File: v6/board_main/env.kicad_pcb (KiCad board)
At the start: 4 copper layers, 57.8 x 34 mm, 187 parts, among them J1 M50-3142045THT, J2 M50-3142045THT, J3 53261-0271, J4 USB4105-GF-A, J5 FEMALE_HEADER_2X1, M1 SISS23DN, M2 SISS23DN, Q1 FDN302P, U1 REF3012AIDBZR, U10 CY7C1051DV33, U2 MCP73833T-AMI/MF, U3 LTC3569EUDPBF, U4 PAC1934, U5 PAC1934, U6 W25Q16JVUXIQ, U7 RP2040, U8 SPARTAN7-LX15, U9 S25FL256S, X1 12MHz, X2 32MHz, X3 100MHz

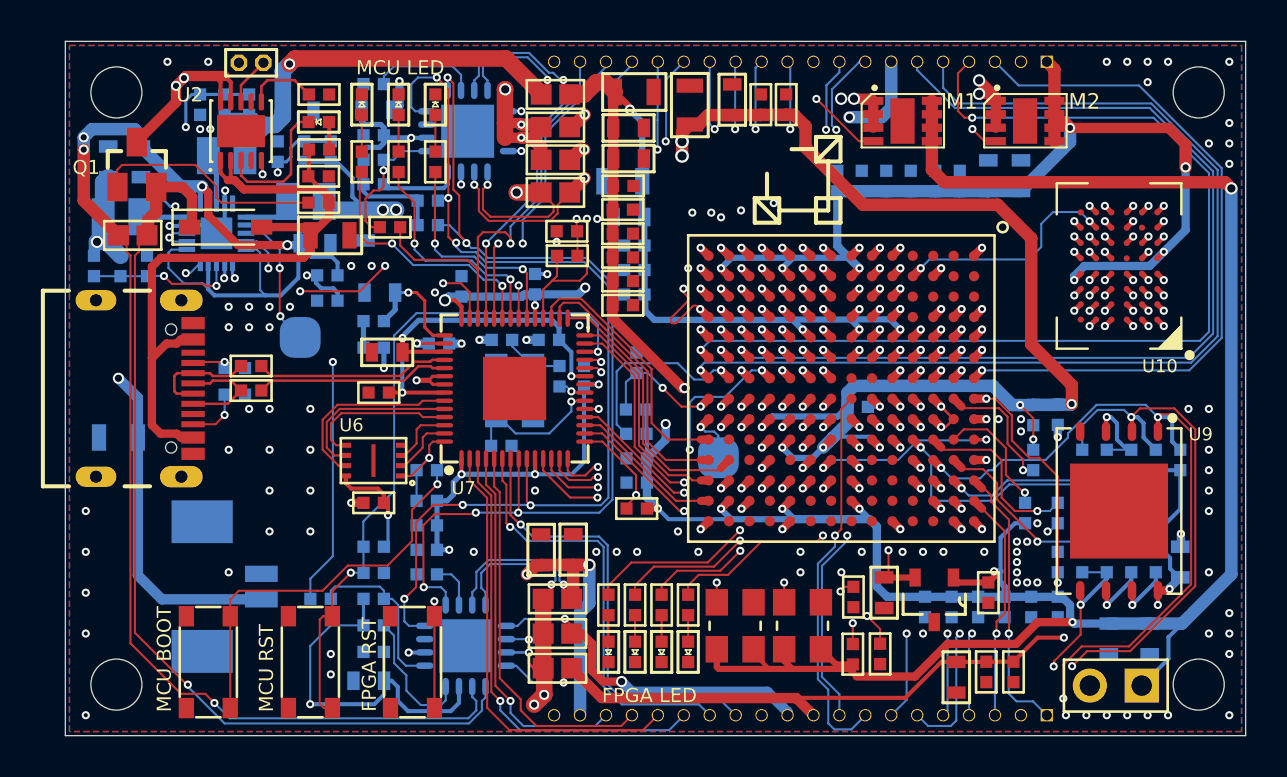
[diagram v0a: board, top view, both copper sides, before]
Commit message: Rephrasing ENV5 design
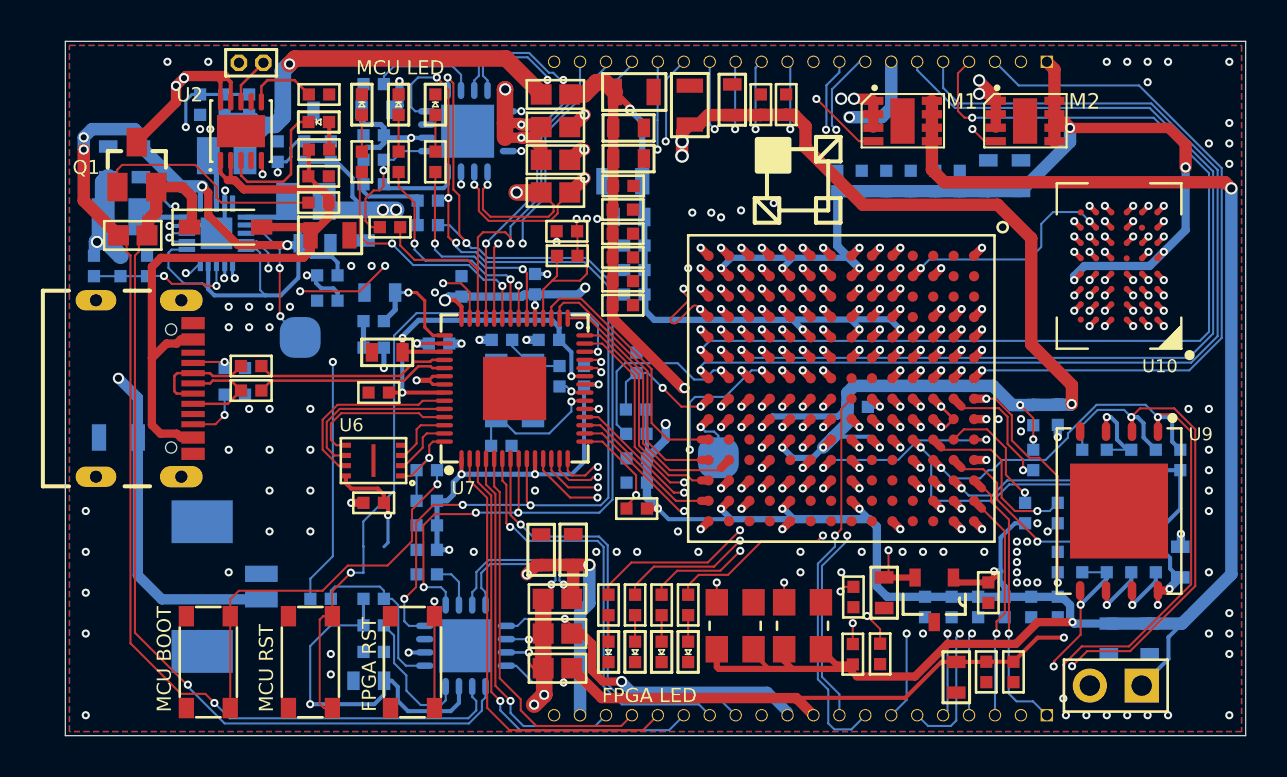
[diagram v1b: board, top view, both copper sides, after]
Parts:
- removed C27: 0.1uF, 0402
- removed R39: 499R, 0402
- removed UNK_HOLE_0: , dummyfp0
- removed UNK_HOLE_1: , dummyfp1
- removed UNK_HOLE_2: , dummyfp2
- removed UNK_HOLE_3: , dummyfp3
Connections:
- net ADC_AVDD renamed /MCU/ADC_AVDD
- net ADC_VREF renamed Net-(R37-Pad1)
- net FPGA_DONE renamed /FPGA/FPGA_DONE
- net FPGA_INT_B renamed /FPGA/FPGA_INT_B
- net FPGA_VCCIO_MON renamed /Power Sensing/FPGA_VCCIO_MON
- net FPGA_VCC_SRAM_MON renamed /Power Sensing/FPGA_VCC_SRAM_MON
- net MCU_1V1 renamed /MCU/MCU_1V1
- net MCU_QSPI_SCLK renamed /MCU/MCU_QSPI_SCLK
- net MCU_QSPI_SD0 renamed /MCU/MCU_QSPI_SD0
- net MCU_QSPI_SD1 renamed /MCU/MCU_QSPI_SD1
- net MCU_QSPI_SD2 renamed /MCU/MCU_QSPI_SD2
- net MCU_QSPI_SD3 renamed /MCU/MCU_QSPI_SD3
- net MCU_QSPI_SS renamed /MCU/MCU_QSPI_SS
- net MCU_USB_D_N renamed /MCU/MCU_USB_D_N
- net MCU_USB_D_P renamed /MCU/MCU_USB_D_P
- net PGOOD renamed /Power Supply/PGOOD
- net PIO0/SPI2FLASH_MISO(SPI0) renamed PIO0/SPI2FLASH_MISO(SPI0)
- net PIO1/SPI2FLASH_CS(SPI0) renamed PIO1/SPI2FLASH_CS(SPI0)
- net PIO10/SPI_SCK(SPI1)/I2C1SDA renamed PIO10/SPI_SCK(SPI1)/I2C1SDA
- net PIO11/SPI_MOSI/I2C1SCL renamed PIO11/SPI_MOSI/I2C1SCL
- net PIO12/~{FPGA_RESET} renamed PIO12/~{FPGA_RESET}
- net PIO13/GPIO2FPGA_0 renamed PIO13/GPIO2FPGA_0
- net PIO14/GPIO2FPGA_1 renamed PIO14/GPIO2FPGA_1
- net PIO15/GPIO2FPGA_2 renamed PIO15/GPIO2FPGA_2
- net PIO16/SPI2FPGA_MISO renamed PIO16/SPI2FPGA_MISO
- net PIO17/SPI2FPGA_CS renamed PIO17/SPI2FPGA_CS
- net PIO18/SPI2FPGA_SCK renamed PIO18/SPI2FPGA_SCK
- net PIO19/SPI2FPGA_MOSI renamed PIO19/SPI2FPGA_MOSI
- net PIO2/SPI2FLASH_SCK(SPI0) renamed PIO2/SPI2FLASH_SCK(SPI0)
- net PIO20/GPIO2FPGA_3 renamed PIO20/GPIO2FPGA_3
- net PIO21/~{PWR_FPGA_IO_SRAM} renamed PIO21/~{PWR_FPGA_IO_SRAM}
- net PIO22/LED0 renamed /MCU/PIO22/LED0
- net PIO23/PWR_ON_1V8_1V renamed PIO23/PWR_ON_1V8_1V
- net PIO24/LED1 renamed /MCU/PIO24/LED1
- net PIO25/LED2 renamed /MCU/PIO25/LED2
- net PIO26/ADC0 renamed PIO26/ADC0
- net PIO27/ADC1 renamed PIO27/ADC1
- net PIO28/ADC2/UART0_TX renamed PIO28/ADC2/UART0_TX
- net PIO29/ADC3/UART0_RX renamed PIO29/ADC3/UART0_RX
- net PIO3/SPI2FLASH_MOSI(SPI0) renamed PIO3/SPI2FLASH_MOSI(SPI0)
- net PIO4/UART1_TX renamed PIO4/UART1_TX
- net PIO5/UART1_RX renamed PIO5/UART1_RX
- net PIO6/I2C1_SDA renamed PIO6/I2C1_SDA
- net PIO7/I2C1_SCL renamed PIO7/I2C1_SCL
- net PIO8/SPI_MISO(SPI1)/I2C0_SDA renamed PIO8/SPI_MISO(SPI1)/I2C0_SDA
- net PIO9/SPI_NSS(SPI1)/I2C0_SCL renamed PIO9/SPI_NSS(SPI1)/I2C0_SCL
- net PUDC_B renamed /FPGA/PUDC_B
- net SPI2FLASH_DQ2 renamed /SRAM_Flash/SPI2FLASH_DQ2
- net SPI2FLASH_DQ3 renamed /SRAM_Flash/SPI2FLASH_DQ3
- net ~{EN_PWR_SRAM} renamed /Power Sensing/~{EN_PWR_SRAM}
- net ~{MCU_RST} renamed /MCU/~{MCU_RST}
- net ~{USB_BOOT} renamed /MCU/~{USB_BOOT}
- J4 pad A8: (no net) -> unconnected-(J4-SBU1-PadA8)
- J4 pad B8: (no net) -> unconnected-(J4-SBU2-PadB8)
- U10 pad A6: (no net) -> Net-(U10-NC-PadA6)
- U10 pad E3: (no net) -> Net-(U10-NC-PadA6)
- U10 pad G2: (no net) -> Net-(U10-NC-PadA6)
- U10 pad H6: (no net) -> Net-(U10-NC-PadA6)
- U2 pad 4: (no net) -> unconnected-(U2-STAT2-Pad4)
- U2 pad 7: (no net) -> unconnected-(U2-~{PG}-Pad7)
- U6 pad 9: (no net) -> unconnected-(U6-PAD-Pad9)
- U8 pad A2: (no net) -> unconnected-(U8-IO_L3N_T0_DQS_34-PadA2)
- U8 pad A3: (no net) -> unconnected-(U8-IO_L2N_T0_34-PadA3)
- U8 pad B1: (no net) -> unconnected-(U8-IO_L5N_T0_34-PadB1)
- U8 pad B2: (no net) -> unconnected-(U8-IO_L5P_T0_34-PadB2)
- U8 pad B3: (no net) -> unconnected-(U8-IO_L3P_T0_DQS_34-PadB3)
- U8 pad C1: (no net) -> unconnected-(U8-IO_L11N_T1_SRCC_34-PadC1)
- U8 pad C14: (no net) -> unconnected-(U8-IO_L11N_T1_SRCC_14-PadC14)
- U8 pad C3: (no net) -> unconnected-(U8-IO_L1N_T0_34-PadC3)
- U8 pad D1: (no net) -> unconnected-(U8-IO_L11P_T1_SRCC_34-PadD1)
- U8 pad D13: (no net) -> unconnected-(U8-IO_L8N_T1_D12_14-PadD13)
- U8 pad D14: (no net) -> unconnected-(U8-IO_L11P_T1_SRCC_14-PadD14)
- U8 pad D3: (no net) -> unconnected-(U8-IO_L1P_T0_34-PadD3)
- U8 pad D4: (no net) -> unconnected-(U8-IO_L7N_T1_34-PadD4)
- U8 pad E11: (no net) -> unconnected-(U8-IO_0_14-PadE11)
- U8 pad E12: (no net) -> unconnected-(U8-IO_L7N_T1_D10_14-PadE12)
- U8 pad E13: (no net) -> unconnected-(U8-IO_L10N_T1_D15_14-PadE13)
- U8 pad F11: (no net) -> unconnected-(U8-IO_L12N_T1_MRCC_14-PadF11)
- U8 pad F12: (no net) -> unconnected-(U8-IO_L7P_T1_D09_14-PadF12)
- U8 pad F13: (no net) -> unconnected-(U8-IO_L10P_T1_D14_14-PadF13)
- U8 pad F14: (no net) -> unconnected-(U8-IO_L9N_T1_DQS_D13_14-PadF14)
- U8 pad G14: (no net) -> unconnected-(U8-IO_L9P_T1_DQS_14-PadG14)
- U8 pad H13: (no net) -> unconnected-(U8-IO_L14P_T2_SRCC_14-PadH13)
- U8 pad H14: (no net) -> unconnected-(U8-IO_L14N_T2_SRCC_14-PadH14)
- U8 pad J13: (no net) -> unconnected-(U8-IO_L18P_T2_D28_14-PadJ13)
- U8 pad J14: (no net) -> unconnected-(U8-IO_L18N_T2_D27_14-PadJ14)
- U8 pad K11: (no net) -> unconnected-(U8-IO_L19P_T3_D26_14-PadK11)
- U8 pad L13: (no net) -> unconnected-(U8-IO_L16N_T2_D31_14-PadL13)
- U8 pad L14: (no net) -> unconnected-(U8-IO_L15N_T2_DQS_DOUT_CSO_B_14-PadL14)
- U8 pad M10: (no net) -> unconnected-(U8-IO_25_14-PadM10)
- U8 pad M11: (no net) -> unconnected-(U8-IO_L20P_T3_D24_14-PadM11)
- U8 pad M14: (no net) -> unconnected-(U8-IO_L21N_T3_DQS_D22_14-PadM14)
- U8 pad N10: (no net) -> unconnected-(U8-IO_L23P_T3_D19_14-PadN10)
- U8 pad N14: (no net) -> unconnected-(U8-IO_L21P_T3_DQS_14-PadN14)
